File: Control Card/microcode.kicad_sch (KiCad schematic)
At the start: 36 parts, among them U1 CY7C1021D, U10 74ACT273, U100 74LVC1G08, U101 74LVC1G32, U102 74LVC2G157, U11 74ACT151, U110 74ACT244, U111 74ACT374, U112 74ACT374, U113 74ACT374, U114 74ACT374, U115 74ACT374, U116 74ACT374, U117 74ACT374, U118 74ACT374, U119 74ACT374, U12 74ACT86, U13 74ACT32, U14 74ACT04, U15 74ACT153, U16 74ACT153, U17 74ACT153, U18 74ACT153, U2 CY7C1021D, U20 74ACT02, U21 74ACT20, U24 74ACT30, U3 CY7C1021D, U44 74ACT11, U5 74ACT273, U53 74ACT04, U6 74ACT273, U61 74ACT32, U7 74ACT273, U8 74ACT273, U9 74ACT273

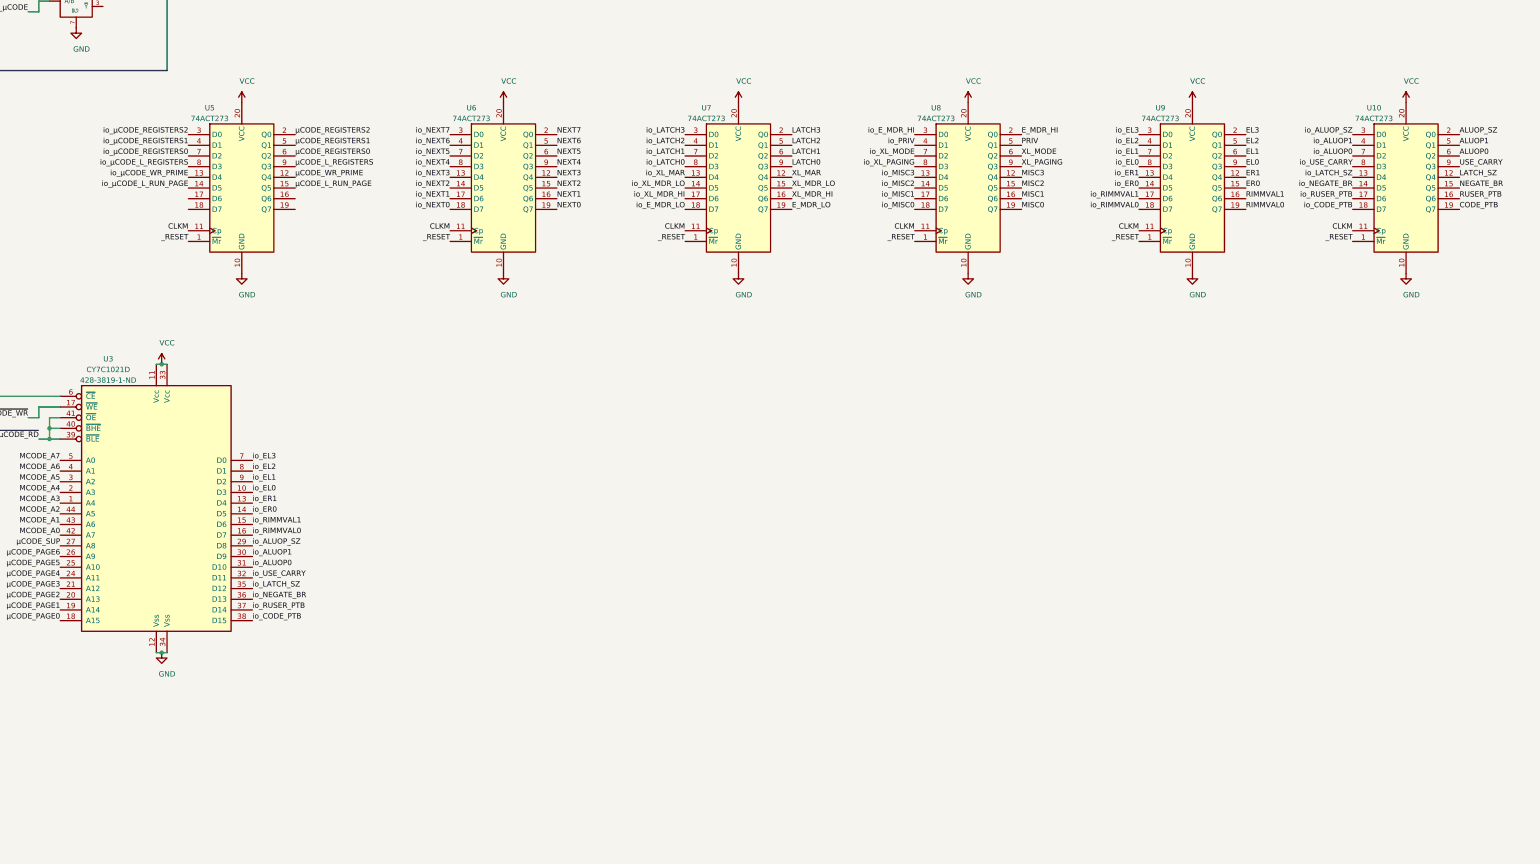
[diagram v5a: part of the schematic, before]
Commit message: move the '273 to save space on the scematic
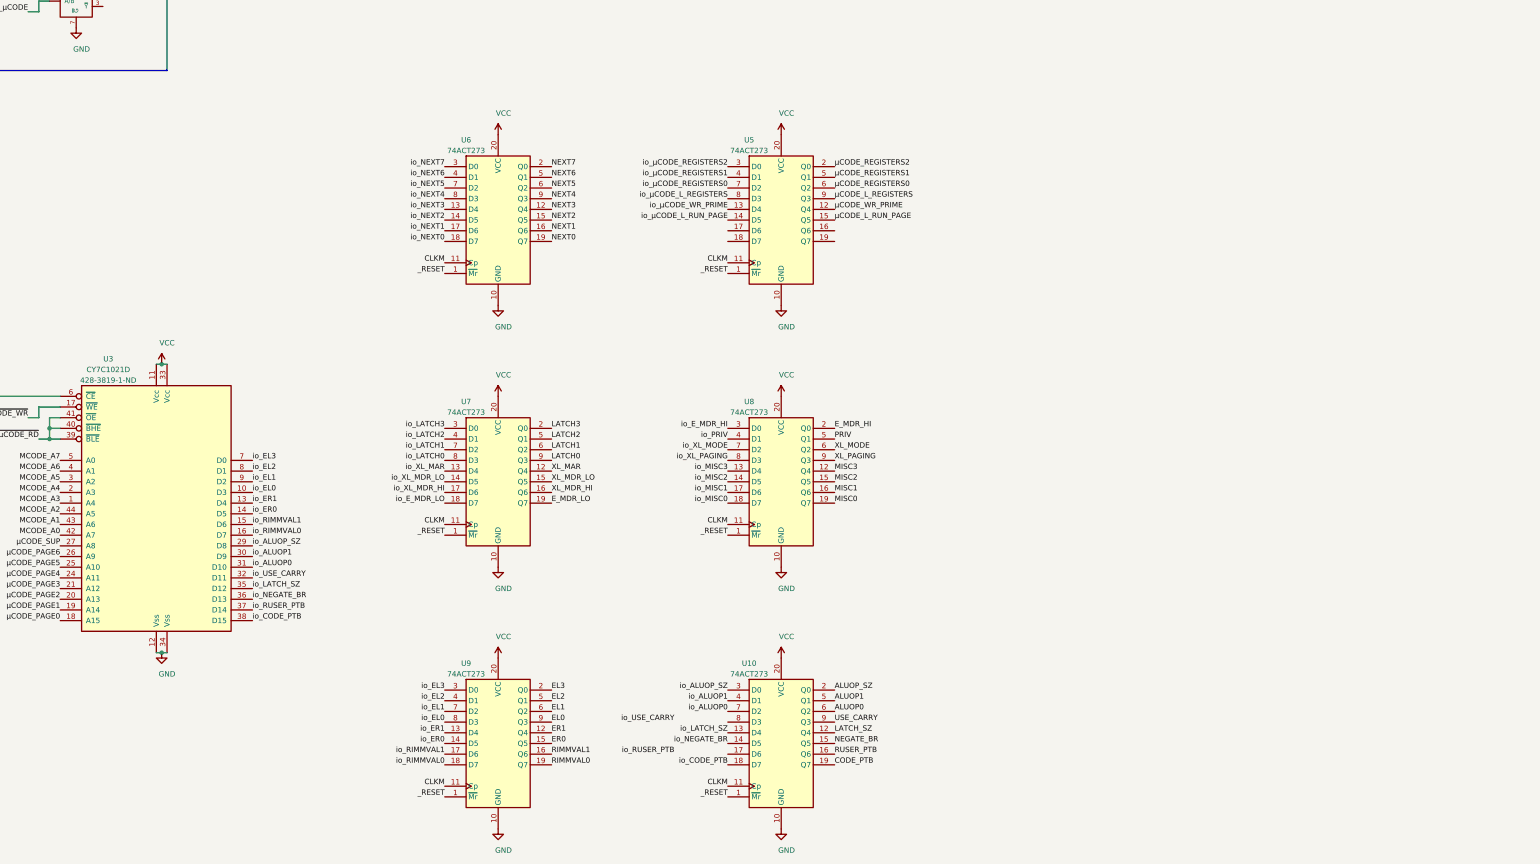
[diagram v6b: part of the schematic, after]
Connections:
- net io_RUSER_PTB: no longer U10.17 (D6)
- net io_USE_CARRY: no longer U10.8 (D3)
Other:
- moved on the sheet: U10, U5, U6, U7, U8, U9

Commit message: add an ESP32 as a service processor
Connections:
- net VCC renamed +5V
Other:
- moved on the sheet: U102
